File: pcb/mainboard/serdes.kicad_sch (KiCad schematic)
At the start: 70 parts, among them J16 SMPM, J17 SMPM, J18 SMPM, J19 SMPM, J20 SMPM, J21 SMPM, J22 SMPM, J23 SMPM, J24 SMPM, J25 SMPM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

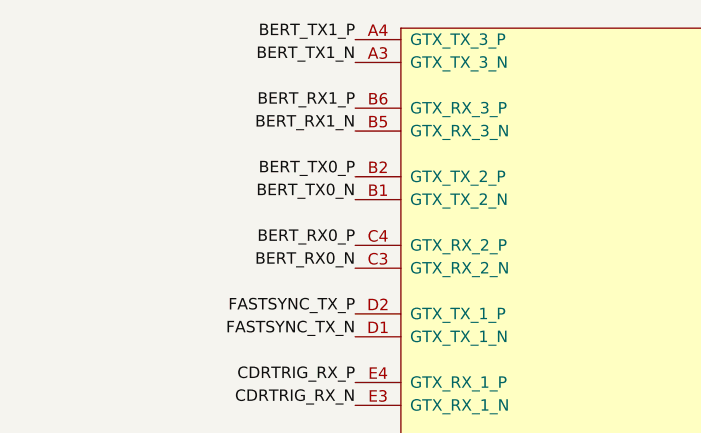
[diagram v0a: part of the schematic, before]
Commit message: Hooked up most input pins
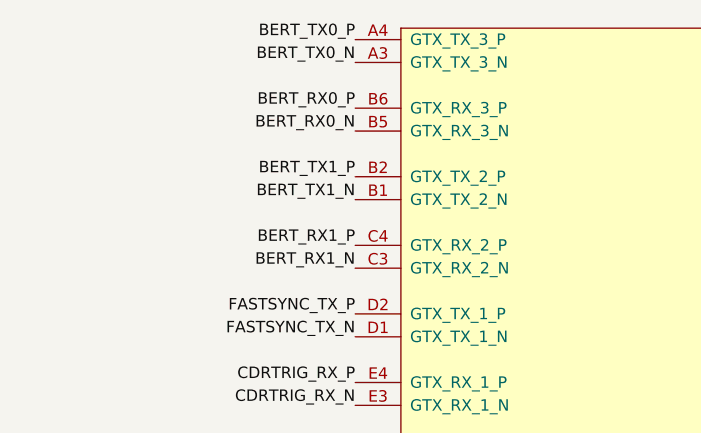
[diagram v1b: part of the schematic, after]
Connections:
- net BERT_RX0_N: now also U8.B5 (GTX_RX_3_N); no longer U8.C3 (GTX_RX_2_N)
- net BERT_RX0_P: now also U8.B6 (GTX_RX_3_P); no longer U8.C4 (GTX_RX_2_P)
- net BERT_RX1_N: now also U8.C3 (GTX_RX_2_N); no longer U8.B5 (GTX_RX_3_N)
- net BERT_RX1_P: now also U8.C4 (GTX_RX_2_P); no longer U8.B6 (GTX_RX_3_P)
- net BERT_TX0_N: now also U8.A3 (GTX_TX_3_N); no longer U8.B1 (GTX_TX_2_N)
- net BERT_TX0_P: now also U8.A4 (GTX_TX_3_P); no longer U8.B2 (GTX_TX_2_P)
- net BERT_TX1_N: now also U8.B1 (GTX_TX_2_N); no longer U8.A3 (GTX_TX_3_N)
- net BERT_TX1_P: now also U8.B2 (GTX_TX_2_P); no longer U8.A4 (GTX_TX_3_P)
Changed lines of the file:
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@@
     (effects (font (size 1.27 1.27)) (justify right bottom))
   )
-  (label "BERT_RX1_N" (at 52.07 29.21 180)
+  (label "BERT_RX1_N" (at 52.07 44.45 180)
     (effects (font (size 1.27 1.27)) (justify right bottom))
   )
@@
     (effects (font (size 1.27 1.27)) (justify right bottom))
   )
-  (label "BERT_TX1_N" (at 52.07 21.59 180)
+  (label "BERT_TX1_N" (at 52.07 36.83 180)
     (effects (font (size 1.27 1.27)) (justify right bottom))
   )
@@
     (effects (font (size 1.27 1.27)) (justify right bottom))
   )
-  (label "BERT_RX0_N" (at 52.07 44.45 180)
+  (label "BERT_RX0_N" (at 52.07 29.21 180)
     (effects (font (size 1.27 1.27)) (justify right bottom))
   )
@@
     (effects (font (size 1.27 1.27)) (justify left bottom))
   )
-  (label "BERT_TX0_N" (at 52.07 36.83 180)
+  (label "BERT_TX0_N" (at 52.07 21.59 180)
     (effects (font (size 1.27 1.27)) (justify right bottom))
   )
@@
     (effects (font (size 1.27 1.27)) (justify right bottom))
   )
-  (label "BERT_TX0_P" (at 52.07 34.29 180)
+  (label "BERT_TX0_P" (at 52.07 19.05 180)
     (effects (font (size 1.27 1.27)) (justify right bottom))
   )
@@
     (effects (font (size 1.27 1.27)) (justify right bottom))
   )
-  (label "BERT_RX1_P" (at 52.07 26.67 180)
+  (label "BERT_RX1_P" (at 52.07 41.91 180)
     (effects (font (size 1.27 1.27)) (justify right bottom))
   )
@@
     (effects (font (size 1.27 1.27)) (justify right bottom))
   )
-  (label "BERT_TX1_P" (at 52.07 19.05 180)
+  (label "BERT_TX1_P" (at 52.07 34.29 180)
     (effects (font (size 1.27 1.27)) (justify right bottom))
   )
@@
     (effects (font (size 1.27 1.27)) (justify right bottom))
   )
-  (label "BERT_RX0_P" (at 52.07 41.91 180)
+  (label "BERT_RX0_P" (at 52.07 26.67 180)
     (effects (font (size 1.27 1.27)) (justify right bottom))
   )

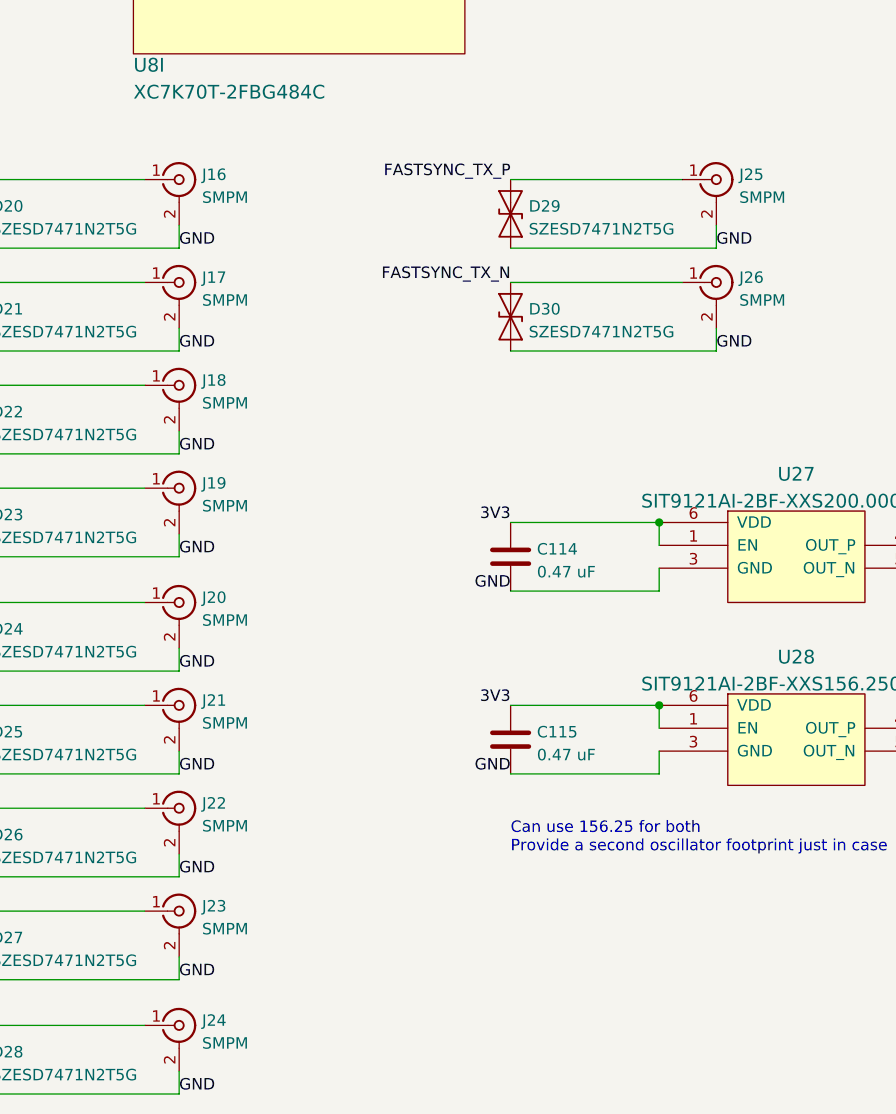
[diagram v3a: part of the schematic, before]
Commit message: Updated schematic with some notes on rework
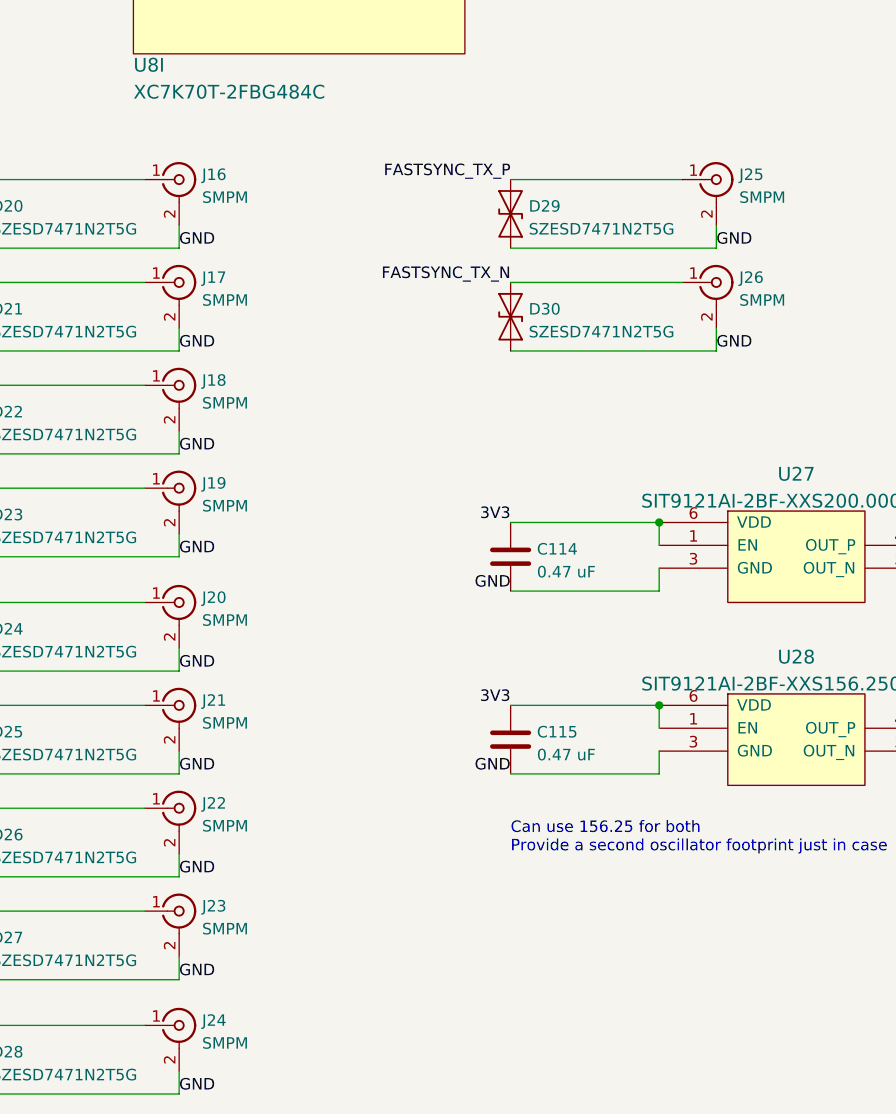
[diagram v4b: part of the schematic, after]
